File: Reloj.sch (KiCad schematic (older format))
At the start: 0 parts

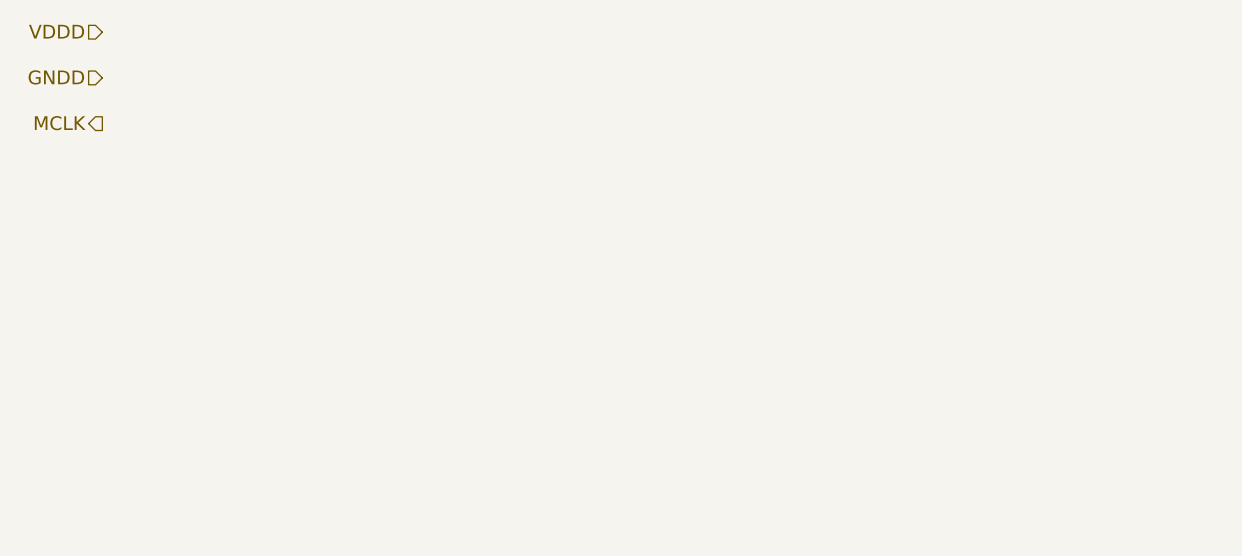
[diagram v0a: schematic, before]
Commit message: Se terminaron todos los simbolos necesarios. Se realizo el esquematico de la fuente y el reloj. Se inicio el esquematico de la parte de señal.
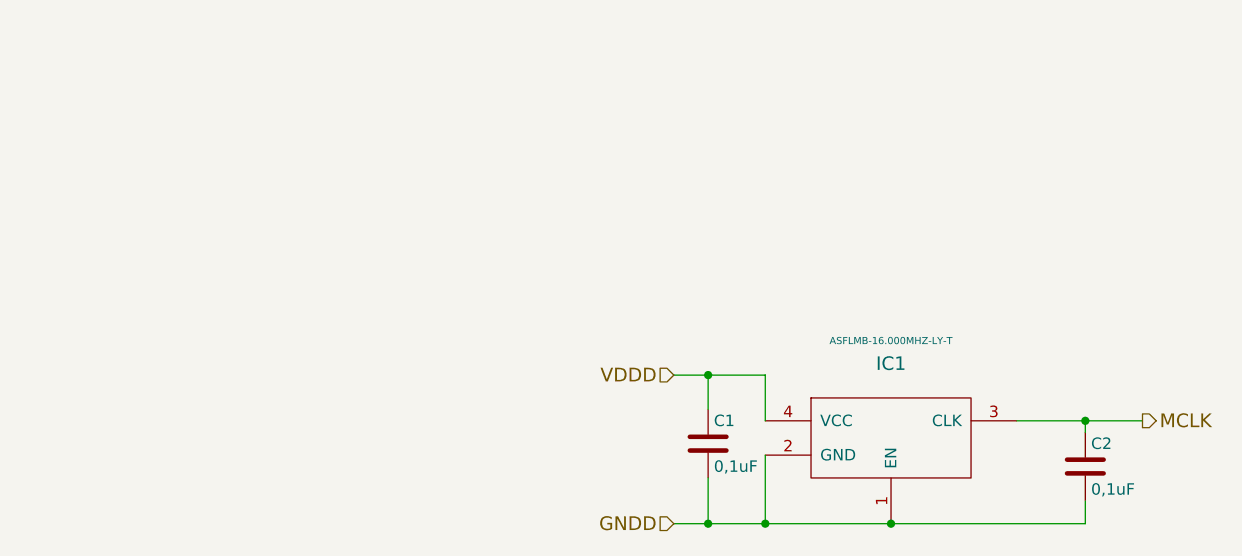
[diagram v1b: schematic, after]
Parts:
- added C1, C2: 0,1uF, symbol C
- added IC1: ASFLMB-16.000MHZ-LY-T, symbol ASFLMB-16.000MHZ-LY-T
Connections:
- net GNDD: now also C1.2, C2.2, IC1.1 (EN), IC1.2 (GND)
- net MCLK: now also C2.1, IC1.3 (CLK)
- net VDDD: now also C1.1, IC1.4 (VCC)
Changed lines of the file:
@@
 LIBS:contrib
 LIBS:valves
+LIBS:PMOD_IA
 LIBS:proyectoDCI-cache
 EELAYER 25 0
@@
 $Descr A4 11693 8268
 encoding utf-8
-Sheet 4 4
+Sheet 3 4
 Title ""
 Date ""
@@
 Comment4 ""
 $EndDescr
-Text HLabel 2500 2100 0    60   Input ~ 0
+Text HLabel 5000 3600 0    60   Input ~ 0
 VDDD
-Text HLabel 2500 2300 0    60   Input ~ 0
+Text HLabel 5000 4250 0    60   Input ~ 0
 GNDD
-Text HLabel 2500 2500 0    60   Output ~ 0
+Text HLabel 7050 3800 2    60   Output ~ 0
 MCLK
+$Comp
+L ASFLMB-16.000MHZ-LY-T IC1
+U 1 1 582F5709
+P 5950 3850
+F 0 "IC1" H 5950 4150 59  0000 C CNN
+F 1 "ASFLMB-16.000MHZ-LY-T" H 5950 4250 31  0000 C CNN
+F 2 "" H 5950 3850 59  0001 C CNN
+F 3 "" H 5950 3850 59  0001 C CNN
+	1    5950 3850
+	1    0    0    -1
+$EndComp
+$Comp
+L C C1
+U 1 1 582F57A1
+P 5150 3900
+F 0 "C1" H 5175 4000 50  0000 L CNN
+F 1 "0,1uF" H 5175 3800 50  0000 L CNN
+F 2 "" H 5188 3750 50  0000 C CNN
+F 3 "" H 5150 3900 50  0000 C CNN
+	1    5150 3900
+	1    0    0    -1
+$EndComp
+$Comp
+L C C2
+U 1 1 582F57DC
+P 6800 4000
+F 0 "C2" H 6825 4100 50  0000 L CNN
+F 1 "0,1uF" H 6825 3900 50  0000 L CNN
+F 2 "" H 6838 3850 50  0000 C CNN
+F 3 "" H 6800 4000 50  0000 C CNN
+	1    6800 4000
+	1    0    0    -1
+$EndComp
+Wire Wire Line
+	5000 3600 5400 3600
+Wire Wire Line
+	5400 3600 5400 3800
+Wire Wire Line
+	5000 4250 6800 4250
+Wire Wire Line
+	5400 4250 5400 3950
+Wire Wire Line
+	5150 4250 5150 4050
+Connection ~ 5150 4250
+Wire Wire Line
+	5150 3750 5150 3600
+Connection ~ 5150 3600
+Connection ~ 5400 4250
+Wire Wire Line
+	6500 3800 7050 3800
+Wire Wire Line
+	6800 3850 6800 3800
+Connection ~ 6800 3800
+Wire Wire Line
+	6800 4250 6800 4150
+Connection ~ 5950 4250
 $EndSCHEMATC

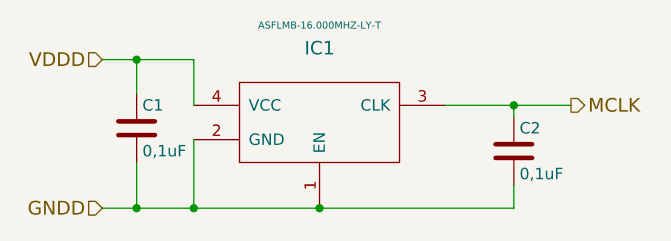
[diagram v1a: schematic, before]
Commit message: Se trabajo sobre la hoja de señal. Se terminó el esquemático, salvo que resta agregar los conectores.
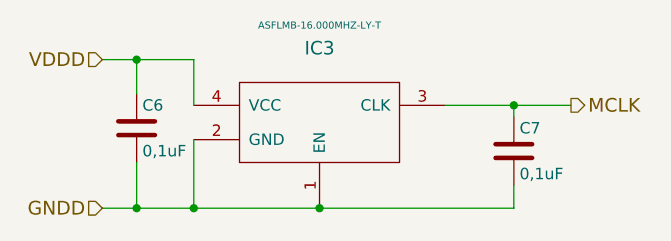
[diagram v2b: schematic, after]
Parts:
- renumbered C1 to C6, C2 to C7, IC1 to IC3
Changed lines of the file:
@@
 LIBS:valves
 LIBS:PMOD_IA
+LIBS:SMA
 LIBS:proyectoDCI-cache
 EELAYER 25 0
@@
 MCLK
 $Comp
-L ASFLMB-16.000MHZ-LY-T IC1
+L ASFLMB-16.000MHZ-LY-T IC3
 U 1 1 582F5709
 P 5950 3850
-F 0 "IC1" H 5950 4150 59  0000 C CNN
+F 0 "IC3" H 5950 4150 59  0000 C CNN
 F 1 "ASFLMB-16.000MHZ-LY-T" H 5950 4250 31  0000 C CNN
 F 2 "" H 5950 3850 59  0001 C CNN
@@
 $EndComp
 $Comp
-L C C1
+L C C6
 U 1 1 582F57A1
 P 5150 3900
-F 0 "C1" H 5175 4000 50  0000 L CNN
+F 0 "C6" H 5175 4000 50  0000 L CNN
 F 1 "0,1uF" H 5175 3800 50  0000 L CNN
 F 2 "" H 5188 3750 50  0000 C CNN
@@
 $EndComp
 $Comp
-L C C2
+L C C7
 U 1 1 582F57DC
 P 6800 4000
-F 0 "C2" H 6825 4100 50  0000 L CNN
+F 0 "C7" H 6825 4100 50  0000 L CNN
 F 1 "0,1uF" H 6825 3900 50  0000 L CNN
 F 2 "" H 6838 3850 50  0000 C CNN

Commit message: Footprints creados y linkeados. Listo para proceder al PCB. Todas las DRC dan OK
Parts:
- C6, C7: footprint (none) -> Capacitors_SMD:C_0805
- IC3: footprint (none) -> propios:TCXO
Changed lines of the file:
@@
 LIBS:PMOD_IA
 LIBS:SMA
+LIBS:sma2
 LIBS:proyectoDCI-cache
 EELAYER 25 0
@@
 F 0 "IC3" H 5950 4150 59  0000 C CNN
 F 1 "ASFLMB-16.000MHZ-LY-T" H 5950 4250 31  0000 C CNN
-F 2 "" H 5950 3850 59  0001 C CNN
+F 2 "propios:TCXO" H 5950 3850 59  0001 C CNN
 F 3 "" H 5950 3850 59  0001 C CNN
 	1    5950 3850
@@
 F 0 "C6" H 5175 4000 50  0000 L CNN
 F 1 "0,1uF" H 5175 3800 50  0000 L CNN
-F 2 "" H 5188 3750 50  0000 C CNN
+F 2 "Capacitors_SMD:C_0805" H 5188 3750 50  0001 C CNN
 F 3 "" H 5150 3900 50  0000 C CNN
 	1    5150 3900
@@
 F 0 "C7" H 6825 4100 50  0000 L CNN
 F 1 "0,1uF" H 6825 3900 50  0000 L CNN
-F 2 "" H 6838 3850 50  0000 C CNN
+F 2 "Capacitors_SMD:C_0805" H 6838 3850 50  0001 C CNN
 F 3 "" H 6800 4000 50  0000 C CNN
 	1    6800 4000

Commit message: Se modificó el esquemático para cumplir con las correcciones propuestas. Resta modificar el rótulo y el símbolo de resistor. Agregar campos KiCost
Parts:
- C6, C7: footprint Capacitors_SMD:C_0805 -> Capacitors_SMD:C_0603
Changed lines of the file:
@@
 encoding utf-8
 Sheet 3 4
-Title ""
-Date ""
-Rev ""
-Comp ""
-Comment1 ""
-Comment2 ""
+Title "Medidor de impedancia (PMOD)"
+Date "2016-11-17"
+Rev "A"
+Comp "CESE - FIUBA"
+Comment1 "Autor: LAROSA, F."
+Comment2 "Revisor: GIGLIOTTI, E."
 Comment3 ""
 Comment4 ""
@@
 F 0 "C6" H 5175 4000 50  0000 L CNN
 F 1 "0,1uF" H 5175 3800 50  0000 L CNN
-F 2 "Capacitors_SMD:C_0805" H 5188 3750 50  0001 C CNN
+F 2 "Capacitors_SMD:C_0603" H 5188 3750 50  0001 C CNN
 F 3 "" H 5150 3900 50  0000 C CNN
 	1    5150 3900
@@
 F 0 "C7" H 6825 4100 50  0000 L CNN
 F 1 "0,1uF" H 6825 3900 50  0000 L CNN
-F 2 "Capacitors_SMD:C_0805" H 6838 3850 50  0001 C CNN
+F 2 "Capacitors_SMD:C_0603" H 6838 3850 50  0001 C CNN
 F 3 "" H 6800 4000 50  0000 C CNN
 	1    6800 4000
